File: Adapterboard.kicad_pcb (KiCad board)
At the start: 2 copper layers, 100 x 100 mm, 72 parts, among them J101 DAC_X, J102 DAC_Y, J103 JTAG, J104 DAC_Z, J105 TUNNEL_IN, J106 Power in +15V, J107 Power in -15V, J108 Power out Preamplifier, J109 Piezo, J110 TUNNEL_1, J111 USB_Connector, U102 DAC X, U103 ESP32-DEVKITC-32D, U104 DAC Y, U106 DAC Z, U107 ADC 8 Click, U108 mint, U109 UniRegensburg, U110 OTH, U201 TL072, U301 TL072

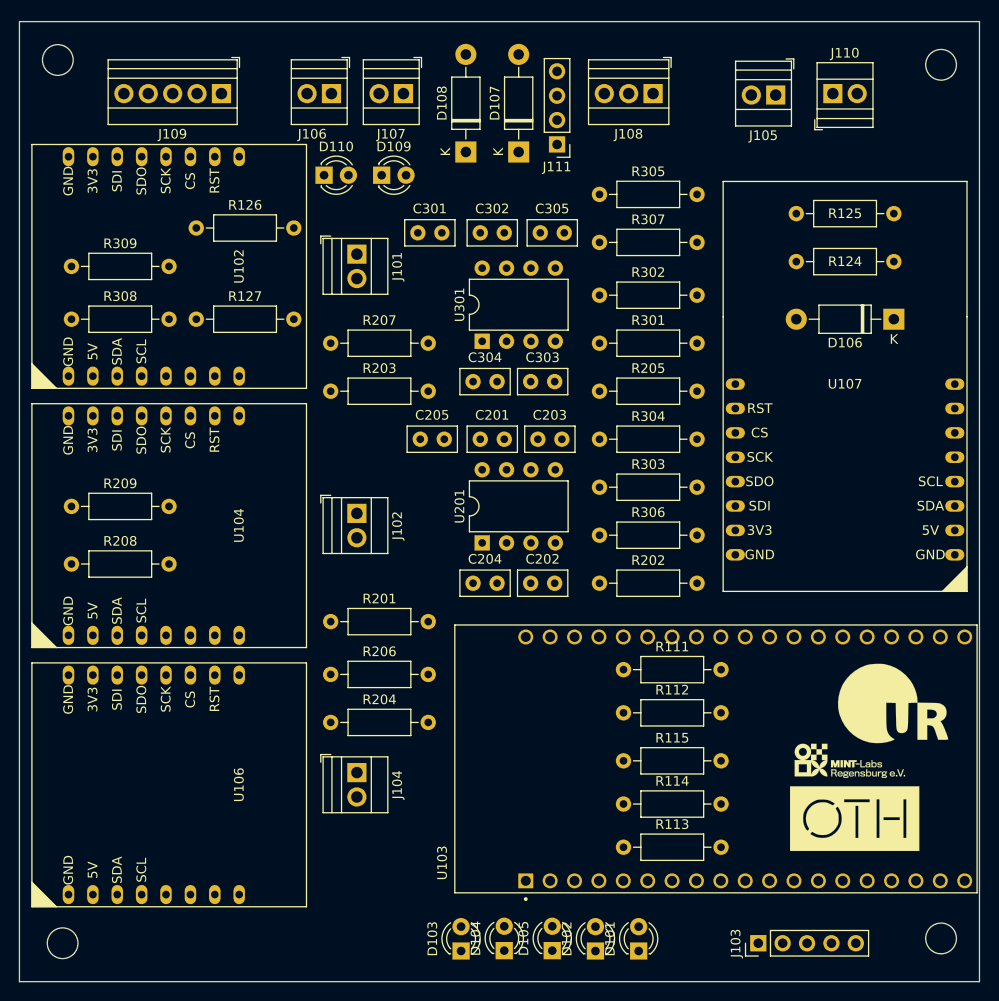
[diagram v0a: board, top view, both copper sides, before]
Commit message: pcb ready. add gnd
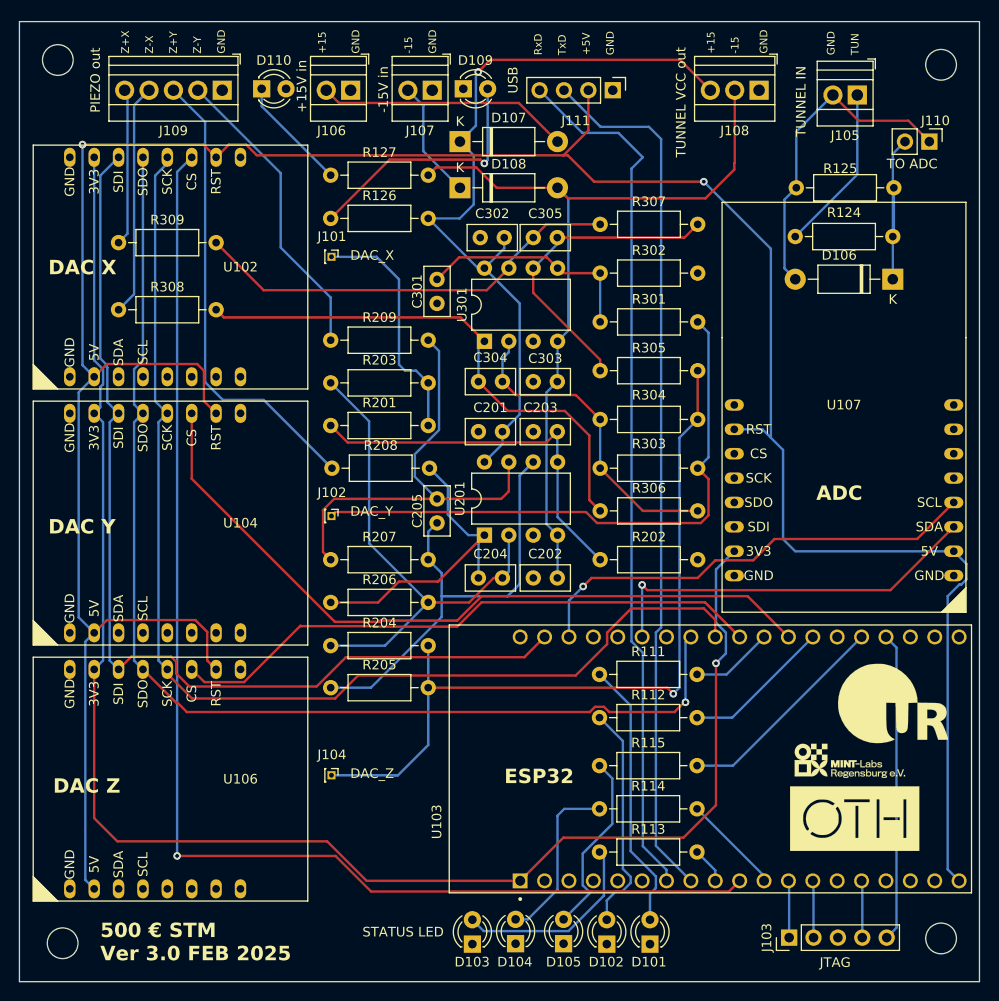
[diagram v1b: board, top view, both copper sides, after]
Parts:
- D104: value LED_YELLOW -> YELLOW
- D105: value LED_GREEN -> GREEN
- D109: value LED_+15V -> LED
- D110: value LED_-15V -> LED
- J101: value DAC_X -> Conn_01x01_Pin; footprint TerminalBlock:TerminalBlock_Xinya_XY308-2.54-2P_1x02_P2.54mm_Horizontal -> Connector_PinHeader_1.00mm:PinHeader_1x01_P1.00mm_Vertical
- J102: value DAC_Y -> Conn_01x01_Pin; footprint TerminalBlock:TerminalBlock_Xinya_XY308-2.54-2P_1x02_P2.54mm_Horizontal -> Connector_PinHeader_1.00mm:PinHeader_1x01_P1.00mm_Vertical
- J104: value DAC_Z -> Conn_01x01_Pin; footprint TerminalBlock:TerminalBlock_Xinya_XY308-2.54-2P_1x02_P2.54mm_Horizontal -> Connector_PinHeader_1.00mm:PinHeader_1x01_P1.00mm_Vertical
- J106: value Power in +15V -> +15V in
- J107: value Power in -15V -> -15V in
- J108: value Power out Preamplifier -> Power to Preamp
- J110: value TUNNEL_1 -> 2xPin; footprint TerminalBlock:TerminalBlock_Xinya_XY308-2.54-2P_1x02_P2.54mm_Horizontal -> Connector_PinHeader_2.54mm:PinHeader_1x02_P2.54mm_Vertical
- J111: value USB_Connector -> 5xPin
- R124: value tbd -> 3K3
- R125: value tbd -> 1K6
- R126, R127, R201, R202, R203, R204, R205, R206, R207, R301, R303, R304, R305, R306, R307: value 3k -> 3K3
- R302: value 3k -> K3
- moved R205 41.7 mm to (82.4, 119.4)
- moved R209 32.1 mm to (82.4, 83.2)
- moved R208 28.9 mm to (82.5, 96.5)
- moved R207 22.5 mm to (82.4, 106.0)
- moved R127 20.5 mm to (82.4, 66.0)
- moved R201 20.4 mm to (82.4, 92.1)
- moved R305 18.4 mm to (110.5, 86.4)
- moved R126 14.0 mm to (82.4, 70.5)
- moved D109 12.4 mm to (96.2, 57.0)
- moved J110 11.2 mm to (144.8, 62.5), turned to -90 degrees
- moved D110 11.1 mm to (75.2, 57.0)
- moved J108 11.1 mm to (127.0, 57.1)
- moved J105 8.50 mm to (137.3, 57.6)
- moved J111 8.10 mm to (111.8, 57.1), turned to -90 degrees
- moved R204 8.00 mm to (82.4, 115.0)
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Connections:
- J109 pad 2: Z-Y -> Z-X
- J109 pad 3: Z+Y -> Z+X
- J109 pad 4: Z-X -> Z+Y
- J109 pad 5: Z+X -> Z-Y
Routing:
- net +5V: track 0.00 -> 289.2 mm, vias 0 -> 2
- net +3V3: track 0.00 -> 169.2 mm, vias 0 -> 1
- net ESP32_CS1: track 0.00 -> 134.0 mm, vias 0 -> 1
- net ESP32_SDO: track 0.00 -> 121.1 mm, vias 0 -> 1
- net ESP32_SCK: track 0.00 -> 120.6 mm
- net ESP32_SDI: track 0.00 -> 104.7 mm
- net TXD: track 0.00 -> 91.2 mm
- net RXD: track 0.00 -> 91.0 mm
- net -15V: track 0.00 -> 85.6 mm
- net Z: track 0.00 -> 82.3 mm, vias 0 -> 1
- net +15V: track 0.00 -> 81.8 mm, vias 0 -> 1
- net ESP32_CS2: track 0.00 -> 78.0 mm
- net ESP32_CS3: track 0.00 -> 62.6 mm
- net Y: track 0.00 -> 61.8 mm
- net /Z+Yr: track 0.00 -> 56.0 mm
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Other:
- board text added: "+15"
- board text added: "+15V in"
- board text added: "+5V"
- board text added: "-15"
- board text added: "-15V in"
- board text added: "500 € STM Ver 3.0 FEB 2025"
- board text added: "ADC"
- board text added: "DAC X"
- board text added: "DAC Y"
- board text added: "DAC Z"
- board text added: "DAC_X"
- board text added: "DAC_Y"
- board text added: "DAC_Z"
- board text added: "ESP32"
- board text added: "GND"
- board text added: "JTAG"
- board text added: "PIEZO out"
- board text added: "RxD"
- board text added: "STATUS LED"
- board text added: "TO ADC"
- board text added: "TUN"
- board text added: "TUNNEL IN"
- board text added: "TUNNEL VCC out"
- board text added: "TxD"
- board text added: "USB"
- board text added: "Z+X"
- board text added: "Z+Y"
- board text added: "Z-X"
- board text added: "Z-Y"
